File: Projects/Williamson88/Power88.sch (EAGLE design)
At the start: 36 parts

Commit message: Added attributes and MPN Created the power circuit
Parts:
- removed CY1, CY2, CY4: 47u, rcl:CPOL-EUE7.5-18
- removed CY3: (no value), rcl:CYYC10B5
- removed CY5, CY6: 1000u, rcl:CPOL-EUE7.5-18
- removed R11, R12: 100k, rcl:R-US_0309/10
- removed R13, R14, R22: 10k, rcl:R-US_0309/10
- removed R15, R16: 1k, rcl:R-US_0309/10
- removed R17, R18: 10, rcl:R-US_0309/10
- removed R19, R20: 10k, pot:TRIM_US-B25P
- removed R21: 680, rcl:R-US_0309/10
- removed V1, V2: 6SN7, tubes:6SN7GT-P
- removed V3, V4: KT88, tubes:KT88-P
- added C12, C5, C6, C7, C8, C9: 220u, rcl:CPOL-EUE7.5-16
- added D1, D10, D11, D12, D2, D3, D4, D5, D6, D7, D8, D9: 1N5408RLG, SamacSys_Parts:1N5408RLG
- added L1, L2, L3: 12H, inductor-bourns:RL622
- C1, C2, C3, C4: value .22uF -> 220u; device rcl:C-EU225-062X268 -> rcl:CPOL-EUE7.5-16; MPN 150224J630LE -> (none); RATING (none) -> 300V
- R1: value (none) -> 100; device pot:TRIM_US-B25P -> rcl:R-EU_R1206
- R10, R9: value 47k -> 10k; device rcl:R-US_0309/10 -> rcl:R-EU_R1206; RATING 2W -> (none); TOL 1p -> (none)
- R2: value 10k -> 100; device rcl:R-US_0309/10 -> rcl:R-EU_R1206
- R3: value 47k -> 100; device rcl:R-US_0309/10 -> rcl:R-EU_R1206
- R4: value 470 -> 100; device rcl:R-US_0309/10 -> rcl:R-EU_R1206
- R5, R6: value 22k -> 100; device rcl:R-US_0309/10 -> rcl:R-EU_R1206; TOL 1p -> (none)
- R7, R8: value 470k -> 100; device rcl:R-US_0309/10 -> rcl:R-EU_R1206
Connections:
- removed net -80V: R19.E, R20.E
- removed net 230V: CY1.+, R3.1
- removed net 320V: CY2.+, R5.1
- removed net 477V: CY4.-, R10.1, R9.2
- removed net FB: CY3.2, R22.2
- removed net HEATERS_M: V1".H2, V2".H2, V3".H2, V4".H2
- removed net HEATERS_P: V1".H1, V2".H1, V3".H1, V4".H1
- removed net N$10: C3.1, R10.2, V2B.TA
- removed net N$11: C4.1, R9.1, V2A.TA
- removed net N$12: C3.2, R11.1, R15.1
- removed net N$13: R15.2, V3G$1.PG
- removed net N$14: C4.2, R12.2, R16.1
- removed net N$15: R16.2, V4G$1.PG
- removed net N$16: CY5.+, R17.2, V3G$1.PK
- removed net N$17: CY6.+, R18.1, V4G$1.PK
- removed net N$18: R13.1, R19.A
- removed net N$19: R2.1, V1A.TG
- removed net N$20: R14.1, R20.A
- removed net N$21: R12.1, R20.S
- removed net N$22: R11.2, R19.S
- removed net N$4: C1.1, R5.2, V1B.TA
- removed net N$6: C1.2, R7.1, V2B.TG
- removed net N$7: C2.2, R8.2, V2A.TG
- removed net N$8: R1.S, R2.2
- removed net N$9: R21.2, V2A.TK, V2B.TK
- removed net T1A: V3G$1.PA
- removed net T2A: V3G$1.PSG
- removed net T3A: V4G$1.PSG
- removed net T4A: V4G$1.PA
- removed net VIN: R1.E
- new net 410VAC_L_1: D2.A, D4.K
- new net 410VAC_R_1: D6.A, D8.K
- new net 410_VAC_L_2: C1.-, C2.+, R9.2
- new net 410_VAC_L_3: D1.A, D3.K
- new net 410_VAC_R_2: C5.-, C6.+, R10.2
- new net 410_VAC_R_3: D5.A, D7.K
- new net 70VAC_1: D10.A, D12.K
- new net 70VAC_2: D11.K, D9.A
- new net L_530V: C4.+, L1.2
- new net L_6SN7_HEATER_N: R2.1
- new net L_6SN7_HEATER_P: R1.2
- new net L_KT88_HEATER_N: R6.1
- new net L_KT88_HEATER_P: R5.2
- new net N$40: C9.-, D11.A, D12.A, L3.1
- new net N$5: C1.+, D1.K, D2.K, L1.1
- new net N_80V: C12.-, L3.2
- new net R_530V: C8.+, L2.2
- new net R_6SN7_HEATER_N: R4.1
- new net R_6SN7_HEATER_P: R3.2
- new net R_KT88_HEATER_N: R8.1
- new net R_KT88_HEATER_P: R7.2
- net GND: now also C12.+, C2.-, C3.-, C6.-, C7.-, C9.+, D10.K, D3.A, D4.A, D7.A, D8.A, D9.K, R1.1, R2.2, R3.1, R5.1, R7.1, R8.2; no longer CY1.-, CY2.-, CY4.+, CY5.-, CY6.-, R1.A, R13.2, R14.2, R17.1, R18.2, R21.1, R7.2, R8.1
- net N$1: now also C7.+, C8.-, R10.1; no longer R3.2, V1A.TA, V1B.TG
- net N$2: now also C5.+, D5.K, D6.K, L2.1; no longer CY3.1, R22.1, R4.1, V1A.TK
- net N$3: now also C3.+, C4.-, R9.1; no longer C2.1, R6.1, V1B.TK
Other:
- note added: "410V AC with central tap"
- note added: "6.3V AC"
- note added: "70V AC"
- note added: "Transformers: 0B4B-668E0_20161214133732"

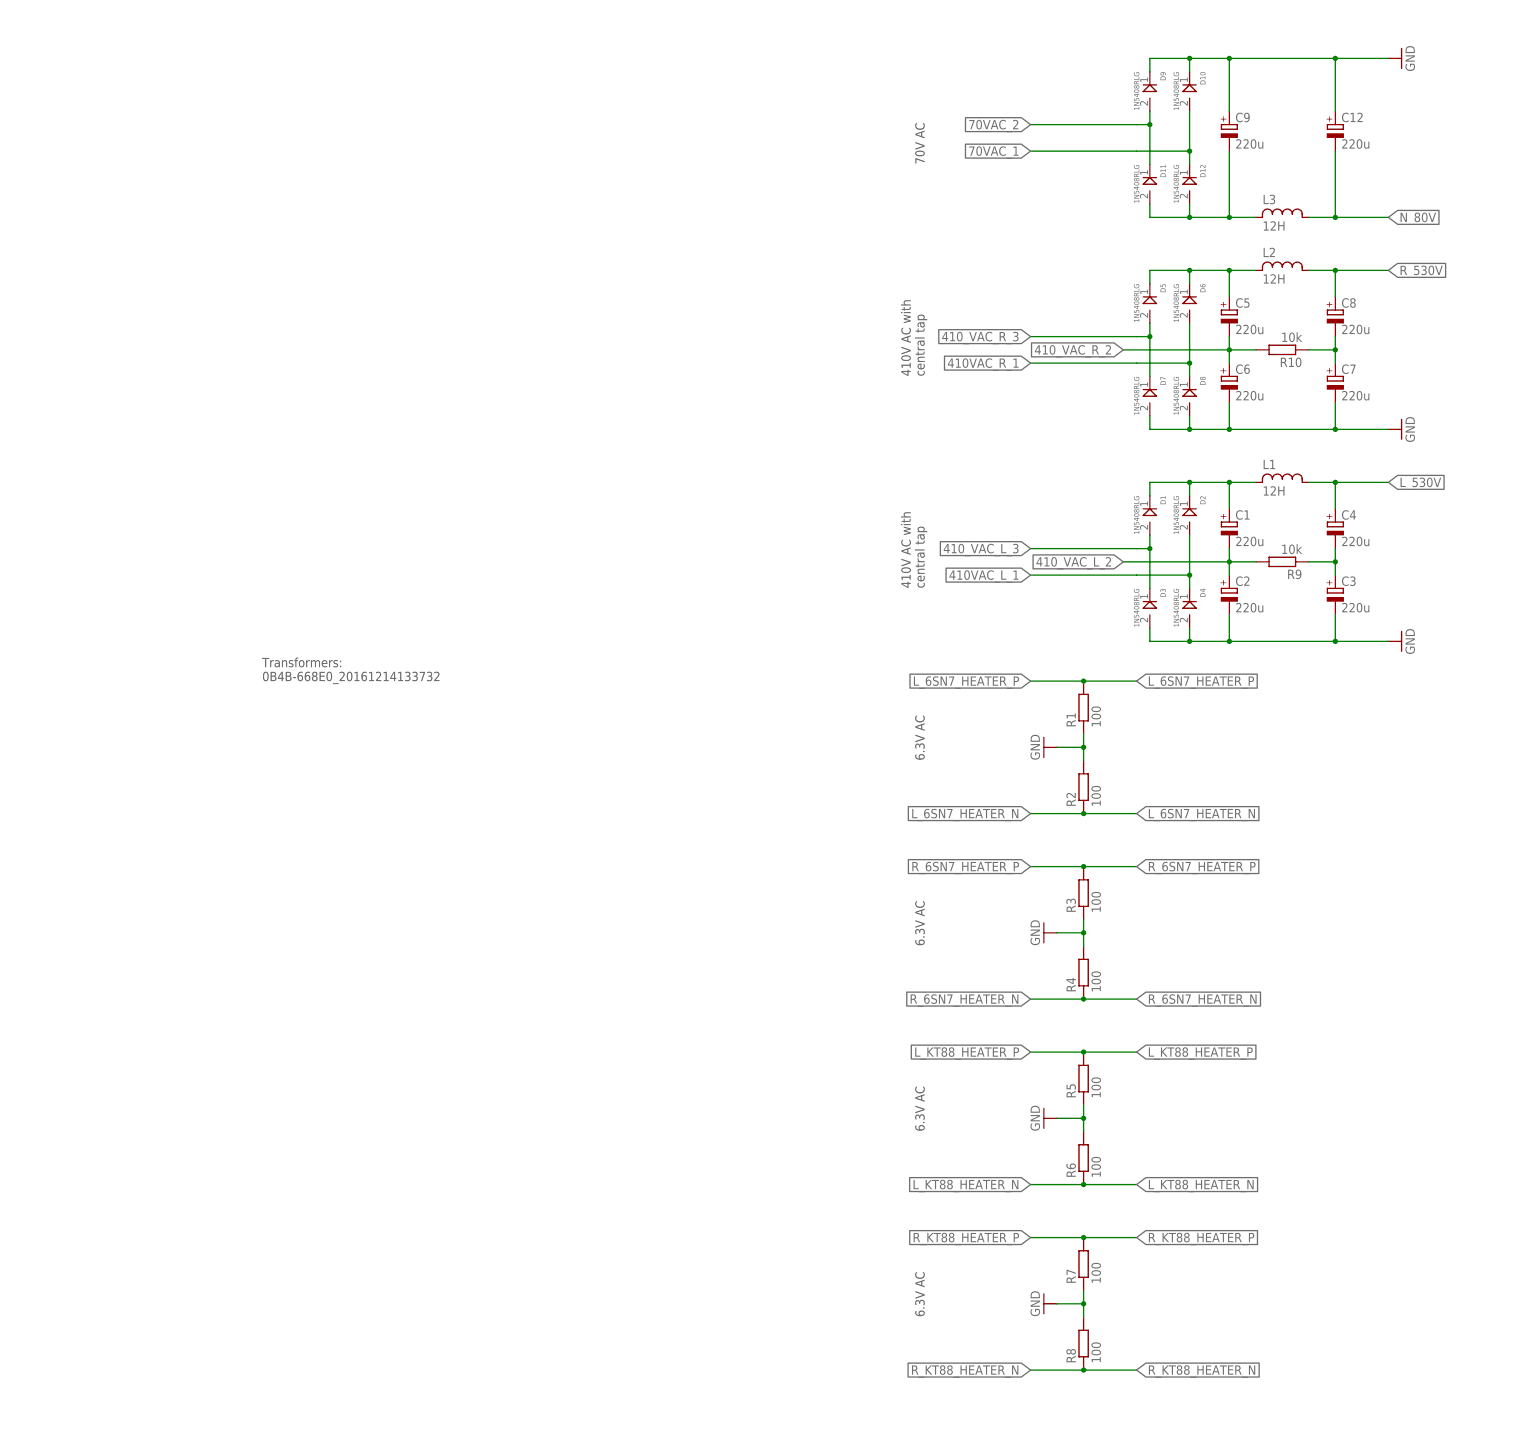
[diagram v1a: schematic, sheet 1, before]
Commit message: Updated power xfer
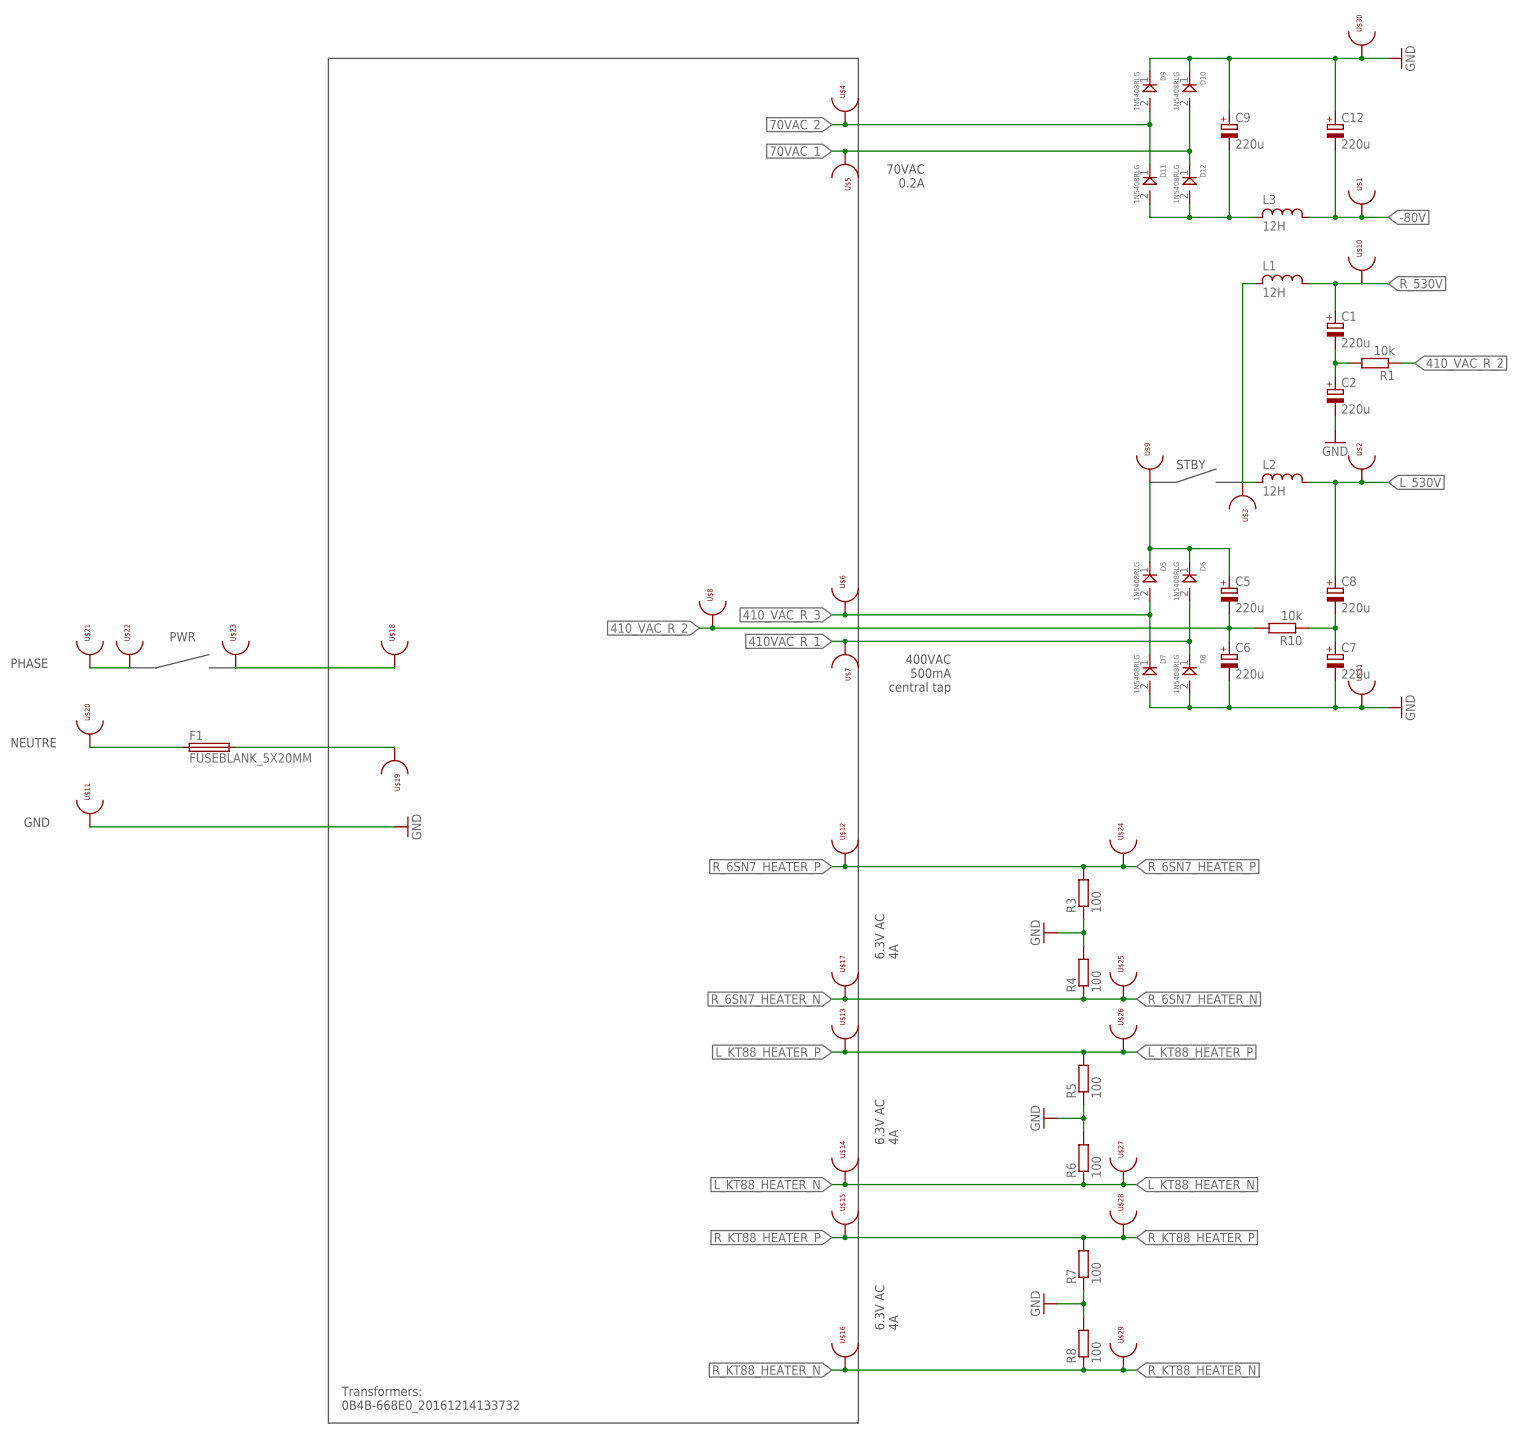
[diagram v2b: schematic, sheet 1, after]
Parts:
- removed C3, C4: 220u, rcl:CPOL-EUE7.5-16
- removed D1, D2, D3, D4: 1N5408RLG, SamacSys_Parts:1N5408RLG
- removed R2: 100, rcl:R-EU_R1206
- removed R9: 10k, rcl:R-EU_R1206
- added F1: FUSEBLANK_5X20MM, fuse:FUSEBLANK_5X20MM
- added U$1, U$10, U$11, U$12, U$13, U$14, U$15, U$16, U$17, U$18, U$19, U$2, U$20, U$21, U$22, U$23, U$24, U$25, U$26, U$27, U$28, U$29, U$3, U$30, U$31, U$4, U$5, U$6, U$7, U$8, U$9: TESTPOINT_HOLE, test_points:TESTPOINT_HOLE
- R1: value 100 -> 10k
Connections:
- removed net 410VAC_L_1: D2.A, D4.K
- removed net 410_VAC_L_2: C1.-, C2.+, R9.2
- removed net 410_VAC_L_3: D1.A, D3.K
- removed net L_6SN7_HEATER_N: R2.1
- removed net L_6SN7_HEATER_P: R1.2
- removed net N$3: C3.+, C4.-, R9.1
- removed net N$5: C1.+, D1.K, D2.K, L1.1
- removed net N_80V: C12.-, L3.2
- new net -80V: C12.-, L3.2, U$1.P$1
- new net 530V: C5.+, D5.K, D6.K, U$9.P$1
- new net AC_PLUG_N: F1.1, U$20.P$1
- new net AC_PLUG_PHASE: U$21.P$1, U$22.P$1
- new net N$4: C1.-, C2.+, R1.2
- new net N$6: F1.2, U$19.P$1
- new net SW_ACIN: U$18.P$1, U$23.P$1
- net 410VAC_R_1: now also U$7.P$1
- net 410_VAC_R_2: now also R1.1, U$8.P$1
- net 410_VAC_R_3: now also U$6.P$1
- net 70VAC_1: now also U$5.P$1
- net 70VAC_2: now also U$4.P$1
- net GND: now also U$11.P$1, U$30.P$1, U$31.P$1; no longer C3.-, D3.A, D4.A, R1.1, R2.2
- net L_530V: now also C8.+, L2.2, U$2.P$1; no longer C4.+, L1.2
- net L_KT88_HEATER_N: now also U$14.P$1, U$27.P$1
- net L_KT88_HEATER_P: now also U$13.P$1, U$26.P$1
- net N$2: now also L1.1, U$3.P$1; no longer C5.+, D5.K, D6.K
- net R_530V: now also C1.+, L1.2, U$10.P$1; no longer C8.+, L2.2
- net R_6SN7_HEATER_N: now also U$17.P$1, U$25.P$1
- net R_6SN7_HEATER_P: now also U$12.P$1, U$24.P$1
- net R_KT88_HEATER_N: now also U$16.P$1, U$29.P$1
- net R_KT88_HEATER_P: now also U$15.P$1, U$28.P$1
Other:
- note added: "400VAC 500mA central tap"
- note added: "6.3V AC 4A"
- note added: "70VAC 0.2A"
- note added: "GND"
- note added: "NEUTRE"
- note added: "PHASE"
- note added: "PWR"
- note added: "STBY"
- note removed: "410V AC with central tap"
- note removed: "6.3V AC"
- note removed: "70V AC"
- moved on the sheet: C1, C2, C5, C6, C7, C8, D5, D6, D7, D8, L1, L2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

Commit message: Cleanup and schematic for the amplifier part
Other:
- note added: "360-0-360 500mA central tap"
- note removed: "400VAC 500mA central tap"
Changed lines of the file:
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@@
 <?xml version="1.0" encoding="utf-8"?>
 <!DOCTYPE eagle SYSTEM "eagle.dtd">
-<eagle version="6.6.0">
+<eagle version="9.1.3">
 <drawing>
 <settings>
 <setting alwaysvectorfont="yes"/>
+<setting keepoldvectorfont="yes"/>
 <setting verticaltext="up"/>
 </settings>
 <grid distance="0.1" unitdist="inch" unit="inch" style="lines" multiple="1" display="no" altdistance="0.01" altunitdist="inch" altunit="inch"/>
 <layers>
-<layer number="1" name="Top" color="4" fill="1" visible="yes" active="no"/>
-<layer number="2" name="Route2" color="1" fill="3" visible="yes" active="no"/>
-<layer number="3" name="Route3" color="4" fill="3" visible="yes" active="no"/>
-<layer number="4" name="Route4" color="1" fill="4" visible="yes" active="no"/>
-<layer number="5" name="Route5" color="4" fill="4" visible="yes" active="no"/>
-<layer number="6" name="Route6" color="1" fill="8" visible="yes" active="no"/>
-<layer number="7" name="Route7" color="4" fill="8" visible="yes" active="no"/>
-<layer number="8" name="Route8" color="1" fill="2" visible="yes" active="no"/>
-<layer number="9" name="Route9" color="4" fill="2" visible="yes" active="no"/>
-<layer number="10" name="Route10" color="1" fill="7" visible="yes" active="no"/>
-<layer number="11" name="Route11" color="4" fill="7" visible="yes" active="no"/>
-<layer number="12" name="Route12" color="1" fill="5" visible="yes" active="no"/>
-<layer number="13" name="Route13" color="4" fill="5" visible="yes" active="no"/>
-<layer number="14" name="Route14" color="1" fill="6" visible="yes" active="no"/>
-<layer number="15" name="Route15" color="4" fill="6" visible="yes" active="no"/>
-<layer number="16" name="Bottom" color="1" fill="1" visible="yes" active="no"/>
-<layer number="17" name="Pads" color="2" fill="1" visible="yes" active="no"/>
-<layer number="18" name="Vias" color="2" fill="1" visible="yes" active="no"/>
-<layer number="19" name="Unrouted" color="6" fill="1" visible="yes" active="no"/>
-<layer number="20" name="Dimension" color="15" fill="1" visible="yes" active="no"/>
-<layer number="21" name="tPlace" color="7" fill="1" visible="yes" active="no"/>
-<layer number="22" name="bPlace" color="7" fill="1" visible="yes" active="no"/>
-<layer number="23" name="tOrigins" color="15" fill="1" visible="yes" active="no"/>
-<layer number="24" name="bOrigins" color="15" fill="1" visible="yes" active="no"/>
-<layer number="25" name="tNames" color="7" fill="1" visible="yes" active="no"/>
-<layer number="26" name="bNames" color="7" fill="1" visible="yes" active="no"/>
-<layer number="27" name="tValues" color="7" fill="1" visible="yes" active="no"/>
-<layer number="28" name="bValues" color="7" fill="1" visible="yes" active="no"/>
+<layer number="1" name="Top" color="4" fill="1" visible="no" active="no"/>
+<layer number="2" name="Route2" color="1" fill="3" visible="no" active="no"/>
+<layer number="3" name="Route3" color="4" fill="3" visible="no" active="no"/>
+<layer number="4" name="Route4" color="1" fill="4" visible="no" active="no"/>
+<layer number="5" name="Route5" color="4" fill="4" visible="no" active="no"/>
+<layer number="6" name="Route6" color="1" fill="8" visible="no" active="no"/>
+<layer number="7" name="Route7" color="4" fill="8" visible="no" active="no"/>
+<layer number="8" name="Route8" color="1" fill="2" visible="no" active="no"/>
+<layer number="9" name="Route9" color="4" fill="2" visible="no" active="no"/>
+<layer number="10" name="Route10" color="1" fill="7" visible="no" active="no"/>
+<layer number="11" name="Route11" color="4" fill="7" visible="no" active="no"/>
+<layer number="12" name="Route12" color="1" fill="5" visible="no" active="no"/>
+<layer number="13" name="Route13" color="4" fill="5" visible="no" active="no"/>
+<layer number="14" name="Route14" color="1" fill="6" visible="no" active="no"/>
+<layer number="15" name="Route15" color="4" fill="6" visible="no" active="no"/>
+<layer number="16" name="Bottom" color="1" fill="1" visible="no" active="no"/>
+<layer number="17" name="Pads" color="2" fill="1" visible="no" active="no"/>
+<layer number="18" name="Vias" color="2" fill="1" visible="no" active="no"/>
+<layer number="19" name="Unrouted" color="6" fill="1" visible="no" active="no"/>
+<layer number="20" name="Dimension" color="15" fill="1" visible="no" active="no"/>
+<layer number="21" name="tPlace" color="7" fill="1" visible="no" active="no"/>
+<layer number="22" name="bPlace" color="7" fill="1" visible="no" active="no"/>
+<layer number="23" name="tOrigins" color="15" fill="1" visible="no" active="no"/>
+<layer number="24" name="bOrigins" color="15" fill="1" visible="no" active="no"/>
+<layer number="25" name="tNames" color="7" fill="1" visible="no" active="no"/>
+<layer number="26" name="bNames" color="7" fill="1" visible="no" active="no"/>
+<layer number="27" name="tValues" color="7" fill="1" visible="no" active="no"/>
+<layer number="28" name="bValues" color="7" fill="1" visible="no" active="no"/>
 <layer number="29" name="tStop" color="7" fill="3" visible="no" active="no"/>
 <layer number="30" name="bStop" color="7" fill="6" visible="no" active="no"/>
@@
 <layer number="35" name="tGlue" color="7" fill="4" visible="no" active="no"/>
 <layer number="36" name="bGlue" color="7" fill="5" visible="no" active="no"/>
-<layer number="37" name="tTest" color="7" fill="1" visible="yes" active="no"/>
-<layer number="38" name="bTest" color="7" fill="1" visible="yes" active="no"/>
+<layer number="37" name="tTest" color="7" fill="1" visible="no" active="no"/>
+<layer number="38" name="bTest" color="7" fill="1" visible="no" active="no"/>
 <layer number="39" name="tKeepout" color="4" fill="11" visible="no" active="no"/>
 <layer number="40" name="bKeepout" color="1" fill="11" visible="no" active="no"/>
@@
 <layer number="44" name="Drills" color="7" fill="1" visible="no" active="no"/>
 <layer number="45" name="Holes" color="7" fill="1" visible="no" active="no"/>
-<layer number="46" name="Milling" color="3" fill="1" visible="yes" active="no"/>
-<layer number="47" name="Measures" color="7" fill="1" visible="yes" active="no"/>
-<layer number="48" name="Document" color="7" fill="1" visible="yes" active="no"/>
-<layer number="49" name="Reference" color="7" fill="1" visible="yes" active="no"/>
-<layer number="51" name="tDocu" color="7" fill="1" visible="yes" active="no"/>
-<layer number="52" name="bDocu" color="7" fill="1" visible="yes" active="no"/>
+<layer number="46" name="Milling" color="3" fill="1" visible="no" active="no"/>
+<layer number="47" name="Measures" color="7" fill="1" visible="no" active="no"/>
+<layer number="48" name="Document" color="7" fill="1" visible="no" active="no"/>
+<layer number="49" name="Reference" color="7" fill="1" visible="no" active="no"/>
+<layer number="51" name="tDocu" color="7" fill="1" visible="no" active="no"/>
+<layer number="52" name="bDocu" color="7" fill="1" visible="no" active="no"/>
 <layer number="88" name="SimResults" color="9" fill="1" visible="yes" active="yes"/>
 <layer number="89" name="SimProbes" color="9" fill="1" visible="yes" active="yes"/>
@@
 <text x="-76.2" y="-160.02" size="1.778" layer="97" rot="R90">6.3V AC
 4A</text>
-<text x="-66.04" y="-30.48" size="1.778" layer="97" rot="R180">400VAC
+<text x="-66.04" y="-30.48" size="1.778" layer="97" rot="R180">360-0-360
 500mA
 central tap</text>
